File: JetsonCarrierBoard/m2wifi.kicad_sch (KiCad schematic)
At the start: 0 parts

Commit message: Added all USB-C components and started M.2 WiFi
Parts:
- added C?: 10u, symbol Device:C
- added C? (x2): (no value), symbol Device:C
- added C?: 0.1u, symbol Device:C
- added J?: (no value), symbol Connector:Bus_M.2_Socket_E
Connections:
- new net +3V3: C?.1, C?.1, C?.2, C?.2, J?.2 (3.3V), J?.4 (3.3V), J?.72 (3.3V), J?.74 (3.3V)
- new net GND: C?.1, C?.1, C?.2, C?.2, J?.1 (GND), J?.18 (GND), J?.33 (GND), J?.39 (GND), J?.45 (GND), J?.51 (GND), J?.57 (GND), J?.63 (GND), J?.69 (GND), J?.7 (GND), J?.75 (GND)
- no-connect marks 0 -> 18

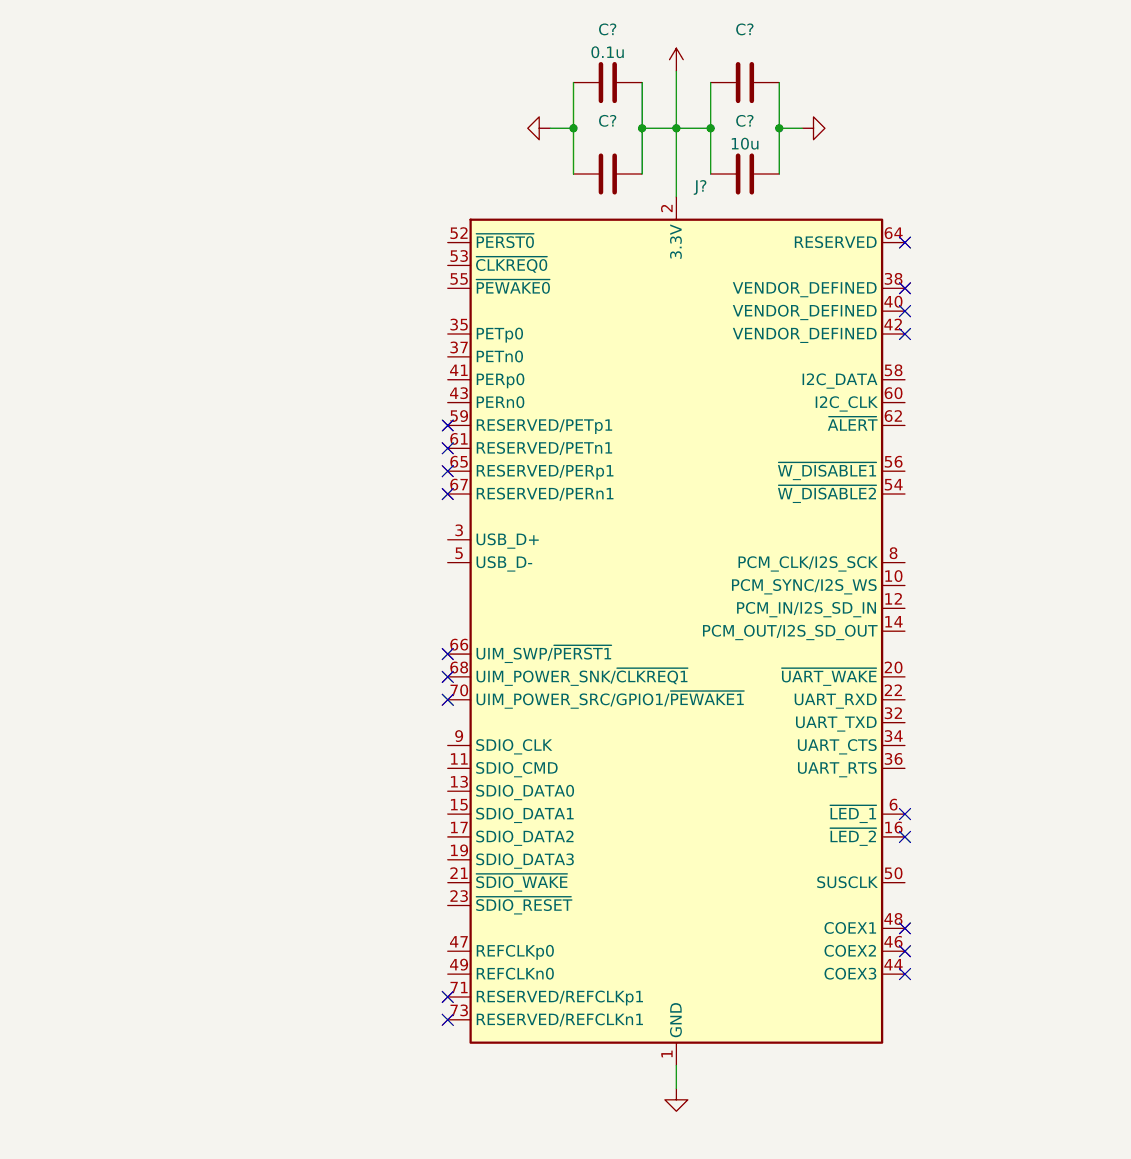
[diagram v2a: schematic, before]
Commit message: Continued M.2 WiFi connections
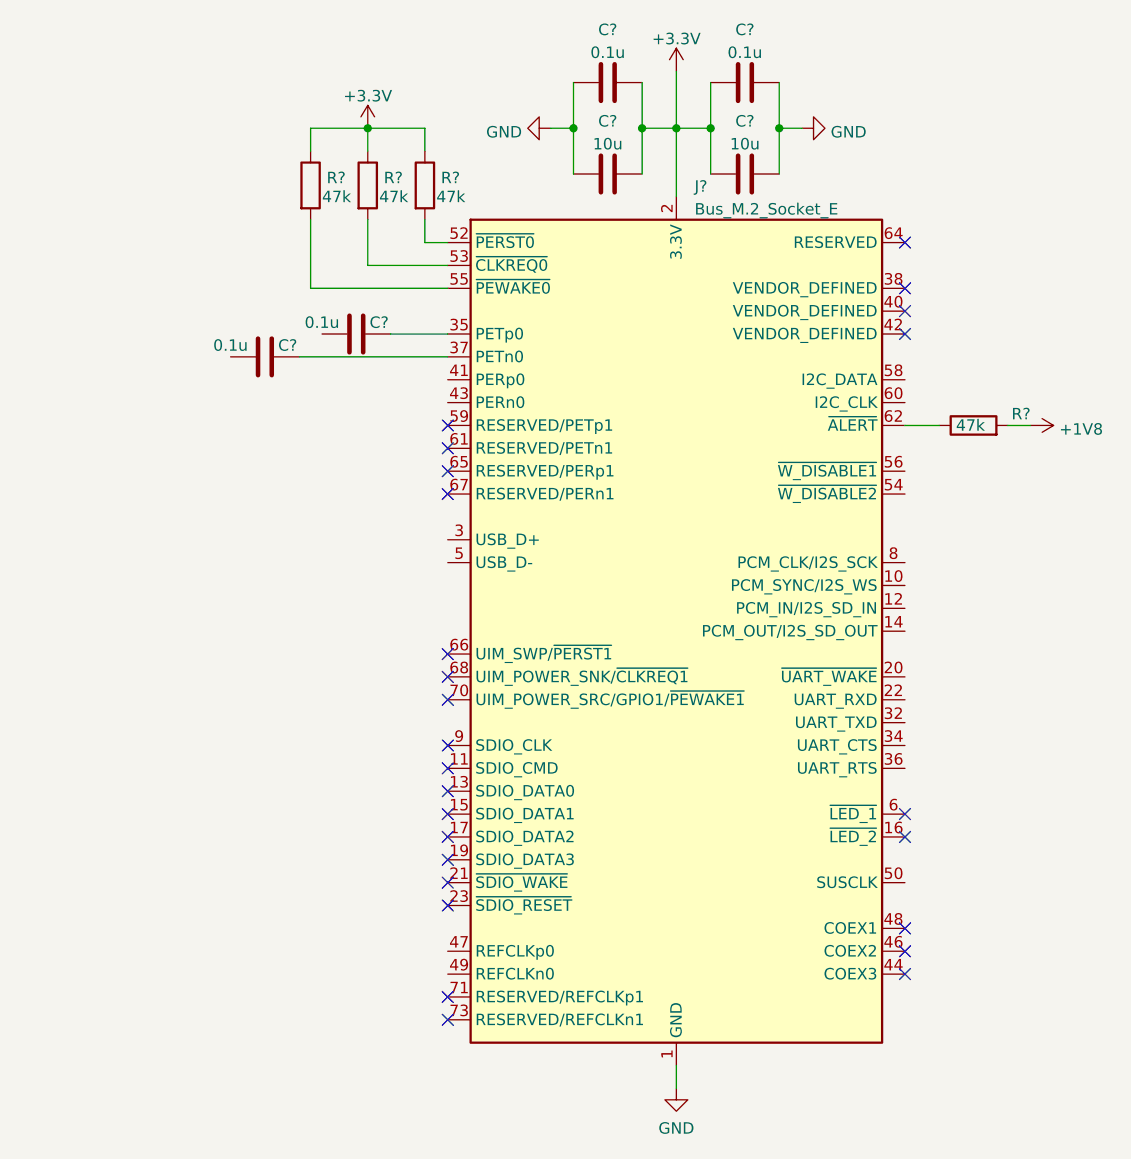
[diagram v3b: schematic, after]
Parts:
- added C? (x2): 0.1u, symbol Device:C
- added R? (x4): 47k, symbol Device:R
- C?: value (none) -> 0.1u
- C?: value (none) -> 10u
- J?: value (none) -> Bus_M.2_Socket_E
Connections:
- net +3V3: now also R?.1, R?.1, R?.1
- net at J?.35 (PETp0): now also C?.2
- net at J?.37 (PETn0): now also C?.2
- net at J?.52 (~{PERST0}): now also R?.2
- net at J?.53 (~{CLKREQ0}): now also R?.2
- net at J?.55 (~{PEWAKE0}): now also R?.2
- net at J?.62 (~{ALERT}): now also R?.1
- new net +1V8: R?.2
- no-connect marks 18 -> 26

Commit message: Finished Basic Wiring WiFi/BT V1
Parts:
- removed R?: 47k, symbol Device:R
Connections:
- net PCIE1_TX0_N: now reaches C?.1
- net PCIE1_TX0_P: now reaches C?.1
- net PCIE1_RST: now reaches J?.52 (~{PERST0}), R?.2
- net PCIE_WAKE: now reaches J?.55 (~{PEWAKE0}), R?.2
- net PCIE1_CLKREQ: now reaches J?.53 (~{CLKREQ0}), R?.2
- net I2S1_LRCK: now reaches J?.10 (PCM_SYNC/I2S_WS)
- net I2S1_SDIN: now reaches J?.12 (PCM_IN/I2S_SD_IN)
- net I2S1_SDOUT: now reaches J?.14 (PCM_OUT/I2S_SD_OUT)
- net USB2_AP_P: now reaches J?.3 (USB_D+)
- net PCIE1_RX0_P: now reaches J?.41 (PERp0)
- net PCIE1_RX0_N: now reaches J?.43 (PERn0)
- net PCIE1_CLK_P: now reaches J?.47 (REFCLKp0)
- net PCIE1_CLK_N: now reaches J?.49 (REFCLKn0)
- net USB2_AP_N: now reaches J?.5 (USB_D-)
- net W_DISABLE1: now reaches J?.56 (~{W_DISABLE1})
- net I2S1_SCLK: now reaches J?.8 (PCM_CLK/I2S_SCK)
- no-connect marks 26 -> 35
